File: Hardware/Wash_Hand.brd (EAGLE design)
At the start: 71.1 x 48.3 mm, 71 parts, among them IC1 LM358D, IC2 LP298XS, IC3 405016TSSOP, J1 I2C, J2 ICSP, J3 SPI, J4 9V_CONN, J5 EXT_VCC, J6 6_PIN_SERIAL_CABLEPTH, Q1 16.0 Mhz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

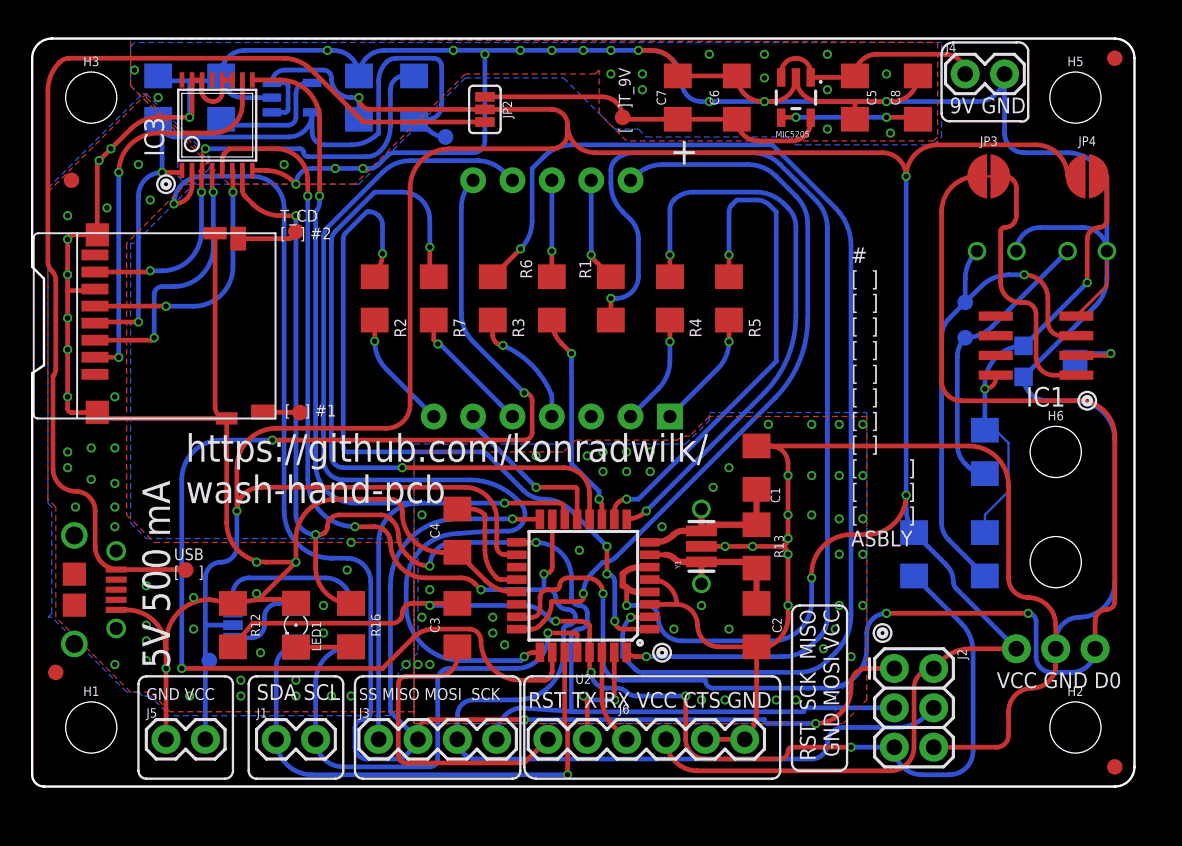
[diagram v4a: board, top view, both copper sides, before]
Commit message: Board: Fixup the registers name and values.
Align the names and values to be next to each other.

Signed-off-by: Konrad Rzeszutek Wilk <konrad@kernel.org>
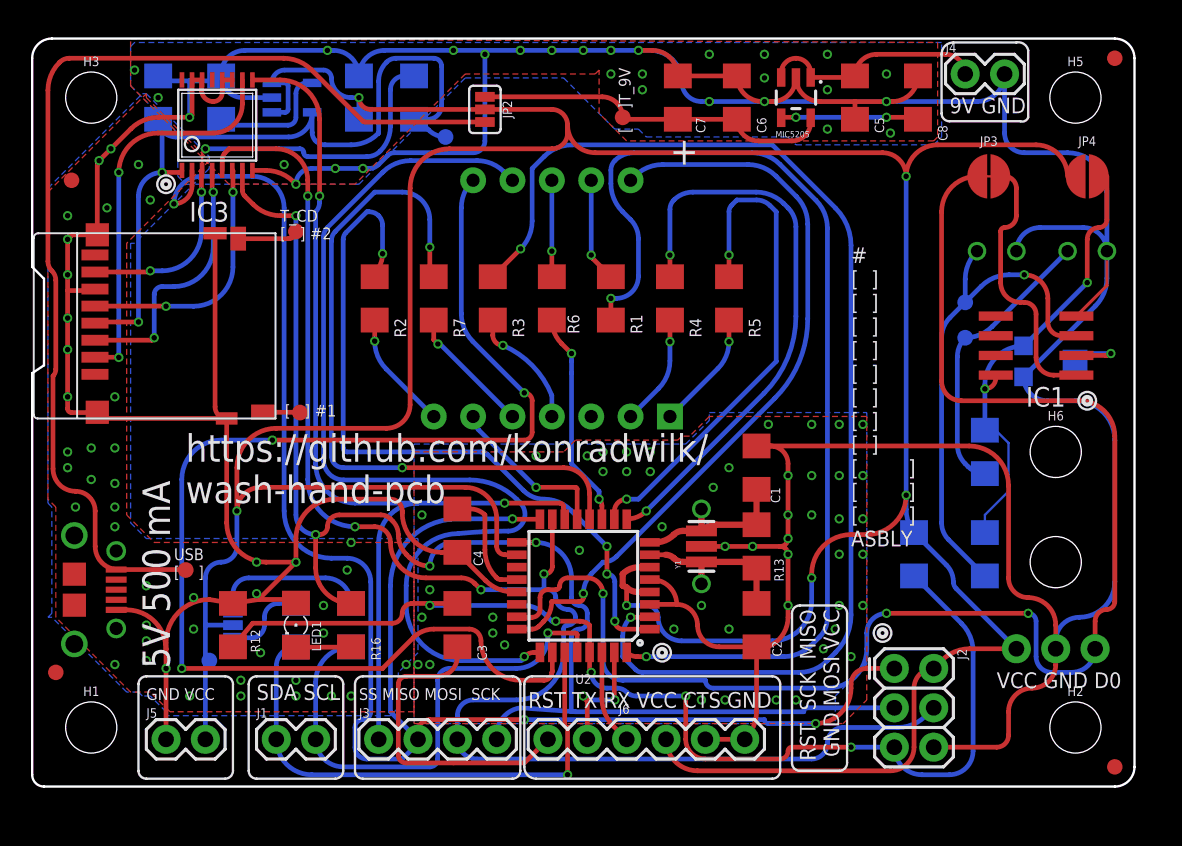
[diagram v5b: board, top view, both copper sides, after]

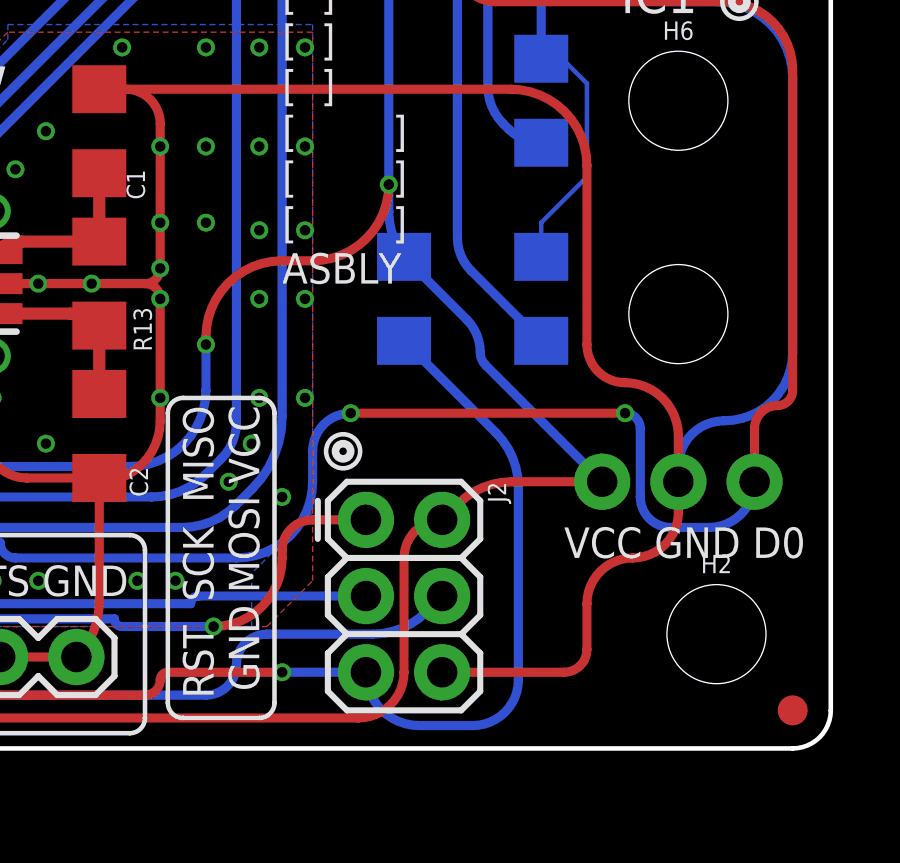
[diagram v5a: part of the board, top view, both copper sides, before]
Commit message: Board: Flip R9 around.
We don't want too many optional components on the back
to easy the production runs (as we have to use red
resin to glue it).

Signed-off-by: Konrad Rzeszutek Wilk <konrad@kernel.org>
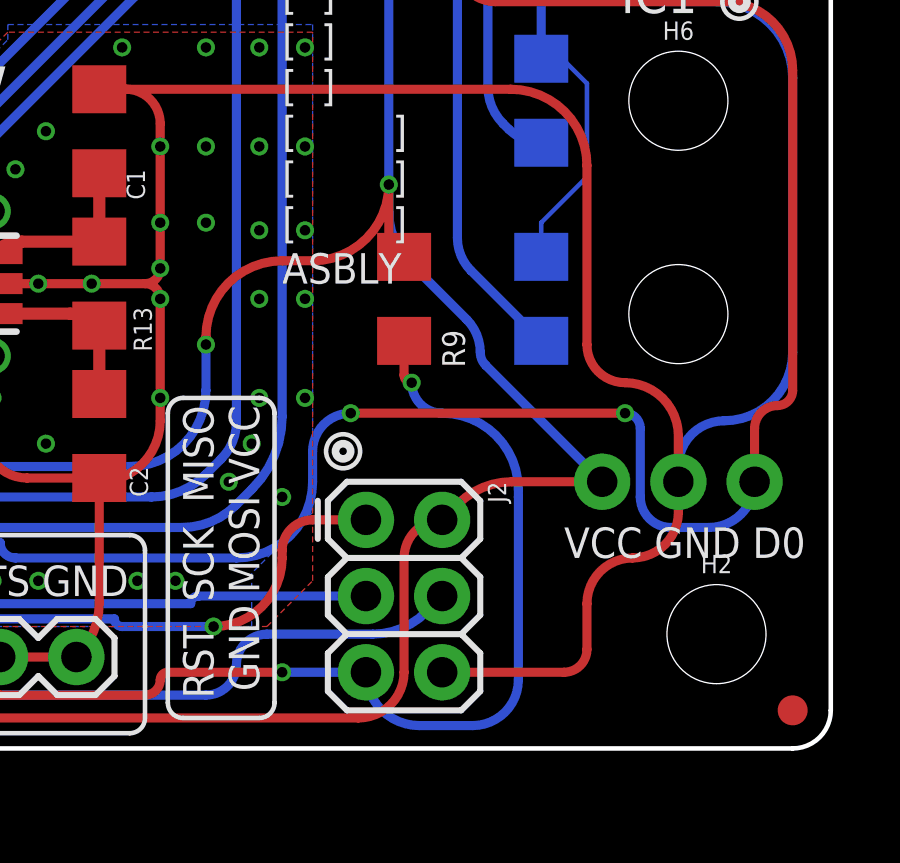
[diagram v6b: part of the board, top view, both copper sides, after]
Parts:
- flipped R9 to the top
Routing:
- net VCC: track 233.9 -> 236.3 mm
- net RESET: track 72.5 -> 72.6 mm, vias 5 -> 6
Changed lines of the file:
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@@
 <attribute name="VALUE" x="27.178" y="33.528" size="0.6096" layer="27" ratio="20" rot="R270"/>
 </element>
-<element name="R9" library="darnok_common" package="1206" value="10K" x="56.896" y="14.986" smashed="yes" rot="MR90">
-<attribute name="NAME" x="54.864" y="12.7" size="0.762" layer="26" ratio="24" rot="MR90"/>
-<attribute name="VALUE" x="55.118" y="15.748" size="0.6096" layer="28" ratio="20" rot="MR90"/>
+<element name="R9" library="darnok_common" package="1206" value="10K" x="56.896" y="14.986" smashed="yes" rot="R90">
+<attribute name="NAME" x="58.928" y="12.7" size="0.762" layer="25" ratio="24" rot="R90"/>
+<attribute name="VALUE" x="58.674" y="15.748" size="0.6096" layer="27" ratio="20" rot="R90"/>
 </element>
 <element name="U$4" library="darnok_usb" package="USB_MICROB_10118194_AMPHENOL" package3d_urn="urn:adsk.eagle:package:21769933/1" value="USB_MICROB_10118194_AMPHENOL" x="1.27" y="12.7" smashed="yes" rot="R270"/>
@@
 <contactref element="J2" pad="5"/>
 <contactref element="R12" pad="2"/>
-<wire x1="60.706" y1="8.723896875" x2="59.96205" y2="10.51995" width="0.3048" layer="16" curve="45"/>
-<wire x1="59.96205" y1="10.51995" x2="56.896" y2="13.586" width="0.3048" layer="16"/>
-<wire x1="60.706" y1="2.286" x2="60.706" y2="8.723896875" width="0.3048" layer="16"/>
+<wire x1="60.706" y1="2.286" x2="60.706" y2="8.382" width="0.3048" layer="16"/>
 <wire x1="23.238" y1="10.538" x2="14.224" y2="10.538" width="0.3048" layer="1"/>
 <wire x1="12.954" y1="9.014" x2="14.224" y2="10.538" width="0.3048" layer="1"/>
@@
 <wire x1="23.876" y1="11.176" x2="23.238" y2="10.538" width="0.3048" layer="1" curve="-90"/>
 <wire x1="25.524" y1="11.814" x2="24.514" y2="11.814" width="0.3048" layer="1"/>
+<wire x1="60.706" y1="8.382" x2="60.706" y2="8.636" width="0.3048" layer="16"/>
+<wire x1="60.706" y1="8.636" x2="58.166" y2="11.176" width="0.3048" layer="16" curve="90"/>
+<wire x1="58.166" y1="11.176" x2="57.15" y2="12.192" width="0.3048" layer="16" curve="-90"/>
+<via x="57.15" y="12.192" extent="1-16" drill="0.35"/>
+<wire x1="57.15" y1="12.192" x2="56.896" y2="12.446" width="0.3048" layer="1" curve="-90"/>
+<wire x1="56.896" y1="12.446" x2="56.896" y2="13.586" width="0.3048" layer="1"/>
 </signal>
 <signal name="VCC">
@@
 <wire x1="58.69205" y1="8.14605" x2="60.488103125" y2="8.89" width="0.3048" layer="1" curve="-45"/>
 <wire x1="60.488103125" y1="8.89" x2="63.5" y2="8.89" width="0.3048" layer="1"/>
-<wire x1="56.896" y1="16.386" x2="57.088" y2="16.194" width="0.3048" layer="16"/>
 <wire x1="57.088" y1="16.194" x2="58.984865625" y2="14.297134375" width="0.3048" layer="16"/>
 <wire x1="58.984865625" y1="14.297134375" x2="59.436" y2="13.208" width="0.3048" layer="16" curve="-45"/>
@@
 <wire x1="64.77" y1="41.402" x2="66.802" y2="39.37" width="0.3048" layer="1" curve="-90"/>
 <wire x1="58.42" y1="41.402" x2="64.77" y2="41.402" width="0.3048" layer="1"/>
+<wire x1="56.388" y1="18.796" x2="56.388" y2="16.894" width="0.3048" layer="1"/>
+<wire x1="56.388" y1="16.894" x2="56.896" y2="16.386" width="0.3048" layer="1" curve="90"/>
 </signal>
 <signal name="0">

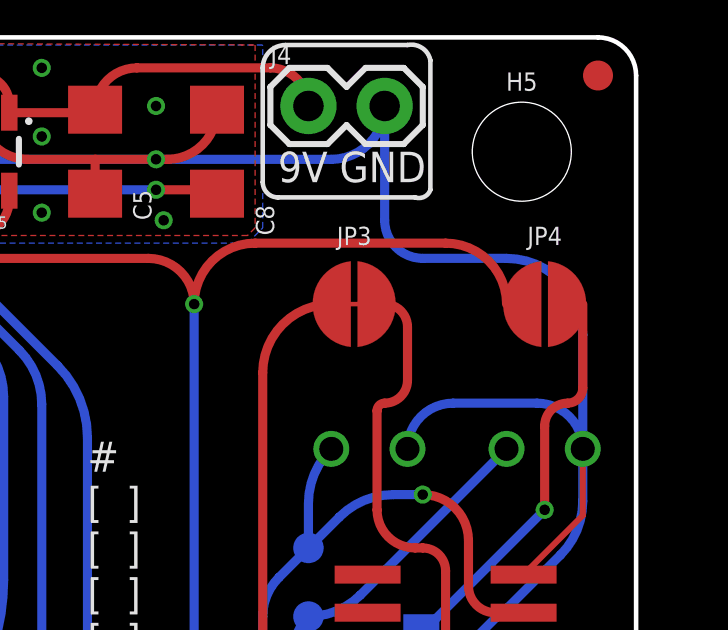
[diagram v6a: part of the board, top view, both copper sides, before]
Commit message: Board/Schematic: Replace open with closed SMT pads for line sensor
As we want it by default enabled.

Signed-off-by: Konrad Rzeszutek Wilk <konrad@kernel.org>
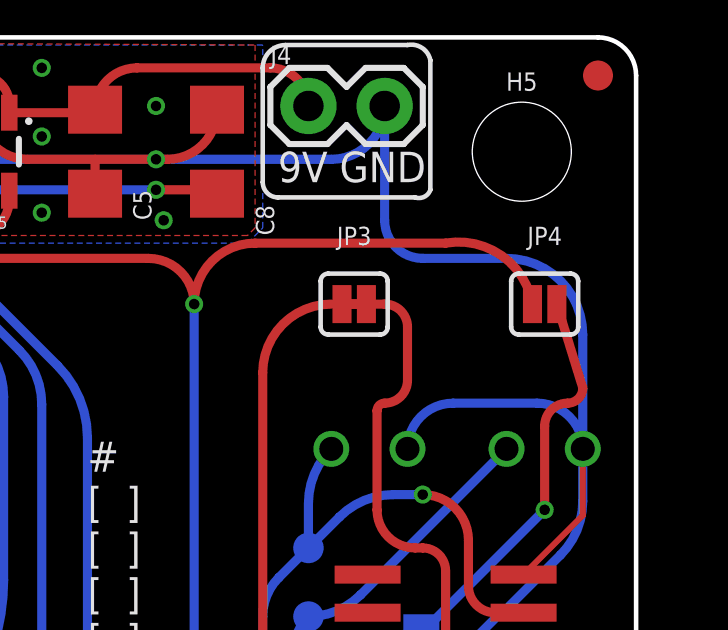
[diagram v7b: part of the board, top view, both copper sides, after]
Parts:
- JP3, JP4: device SparkFun-Jumpers:SMT-JUMPER_2_NO_NO-SILK_ROUND -> SparkFun-Jumpers:SMT-JUMPER_2_NC_PASTE_SILK
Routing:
- net VCC: track 236.3 -> 237.0 mm
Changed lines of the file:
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@@
 <attribute name="VALUE" x="27.432" y="43.688" size="0.6096" layer="27" font="vector" ratio="20" rot="R90" align="top-center"/>
 </element>
-<element name="JP3" library="SparkFun-Jumpers" library_urn="urn:adsk.eagle:library:528" package="SMT-JUMPER_2_NO_NO-SILK_ROUND" package3d_urn="urn:adsk.eagle:package:39278/1" value="ENA_INT_D0" x="61.722" y="39.37" smashed="yes">
+<element name="JP3" library="SparkFun-Jumpers" library_urn="urn:adsk.eagle:library:528" package="SMT-JUMPER_2_NC_PASTE_SILK" package3d_urn="urn:adsk.eagle:package:39282/1" value="ENA_INT_D0" x="61.722" y="39.37" smashed="yes">
 <attribute name="NAME" x="61.722" y="41.3385" size="0.6096" layer="25" font="vector" ratio="20" align="bottom-center"/>
 <attribute name="VALUE" x="61.722" y="37.4015" size="0.6096" layer="27" font="vector" ratio="20" align="top-center"/>
 </element>
-<element name="JP4" library="SparkFun-Jumpers" library_urn="urn:adsk.eagle:library:528" package="SMT-JUMPER_2_NO_NO-SILK_ROUND" package3d_urn="urn:adsk.eagle:package:39278/1" value="ENA_INT_SENSOR" x="68.072" y="39.37" smashed="yes">
+<element name="JP4" library="SparkFun-Jumpers" library_urn="urn:adsk.eagle:library:528" package="SMT-JUMPER_2_NC_PASTE_SILK" package3d_urn="urn:adsk.eagle:package:39282/1" value="ENA_INT_SENSOR" x="68.072" y="39.37" smashed="yes">
 <attribute name="NAME" x="68.072" y="41.3385" size="0.6096" layer="25" font="vector" ratio="20" align="bottom-center"/>
 <attribute name="VALUE" x="68.072" y="37.4015" size="0.6096" layer="27" font="vector" ratio="20" align="top-center"/>
@@
 <wire x1="52.832" y1="16.256" x2="53.848" y2="16.256" width="0.3048" layer="1"/>
 <wire x1="56.388" y1="39.37" x2="58.42" y2="41.402" width="0.3048" layer="1" curve="-90"/>
-<wire x1="64.77" y1="41.402" x2="66.802" y2="39.37" width="0.3048" layer="1" curve="-90"/>
+<wire x1="64.77" y1="41.402" x2="67.6656" y2="39.37" width="0.3048" layer="1" curve="-90"/>
 <wire x1="58.42" y1="41.402" x2="64.77" y2="41.402" width="0.3048" layer="1"/>
 <wire x1="56.388" y1="18.796" x2="56.388" y2="16.894" width="0.3048" layer="1"/>
@@
 <wire x1="67.31" y1="26.543" x2="67.37" y2="26.543" width="0.1524" layer="1"/>
 <contactref element="JP3" pad="2"/>
-<wire x1="60.452" y1="39.37" x2="60.96" y2="39.37" width="0.1524" layer="1"/>
-<wire x1="60.96" y1="39.37" x2="62.738" y2="39.37" width="0.1524" layer="1"/>
-<wire x1="62.738" y1="39.37" x2="62.992" y2="39.37" width="0.1524" layer="1"/>
+<wire x1="61.3156" y1="39.37" x2="60.96" y2="39.37" width="0.1524" layer="1"/>
 <wire x1="31.34465625" y1="10.922" x2="31.2674" y2="10.954" width="0.3048" layer="1" curve="-45"/>
 <wire x1="68.58" y1="8.89" x2="67.056" y2="7.366" width="0.3048" layer="16" curve="-90"/>
@@
 <wire x1="58.674" y1="37.084" x2="60.96" y2="39.37" width="0.3048" layer="1" curve="-90"/>
 <wire x1="58.674" y1="26.162" x2="58.674" y2="37.084" width="0.3048" layer="1"/>
+<wire x1="61.3156" y1="39.37" x2="62.738" y2="39.37" width="0.3048" layer="1"/>
+<wire x1="62.1284" y1="39.37" x2="61.3156" y2="39.37" width="0.3048" layer="1"/>
 </signal>
 <signal name="SDA">
@@
 <wire x1="61.468" y1="25.939" x2="61.468" y2="25.654" width="0.3048" layer="16"/>
 <wire x1="61.468" y1="22.99" x2="61.468" y2="25.654" width="0.3048" layer="16"/>
-<wire x1="69.342" y1="39.37" x2="69.342" y2="36.576" width="0.3048" layer="1"/>
+<wire x1="68.4784" y1="39.37" x2="69.342" y2="36.576" width="0.3048" layer="1"/>
 <wire x1="69.342" y1="36.576" x2="68.834" y2="36.068" width="0.3048" layer="1" curve="-90"/>
 <wire x1="68.834" y1="36.068" x2="68.072" y2="35.306" width="0.3048" layer="1" curve="90"/>

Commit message: Board/Schematic: Replace 9V/5V SMT pad with normally closed
Makes it easier to debug as the solder will close both
of. But if we are doing production runs we would enable/disable
the connectors by not populating the components (like the
whole 9V power-plant).

Signed-off-by: Konrad Rzeszutek Wilk <konrad@kernel.org>
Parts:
- JP2: device SparkFun-Jumpers:SMT-JUMPER_3_1-NC_PASTE_SILK -> SparkFun-Jumpers:SMT-JUMPER_3_2-NC_PASTE_SILK
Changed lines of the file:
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@@
 <attribute name="VALUE" x="59.436" y="42.164" size="0.6096" layer="27" font="vector" ratio="20"/>
 </element>
-<element name="JP2" library="SparkFun-Jumpers" library_urn="urn:adsk.eagle:library:528" package="SMT-JUMPER_3_1-NC_PASTE_SILK" package3d_urn="urn:adsk.eagle:package:39293/1" value="9V_JUMPER" x="29.21" y="43.688" smashed="yes" rot="R270">
+<element name="JP2" library="SparkFun-Jumpers" library_urn="urn:adsk.eagle:library:528" package="SMT-JUMPER_3_2-NC_PASTE_SILK" package3d_urn="urn:adsk.eagle:package:39294/1" value="9V_JUMPER" x="29.21" y="43.688" smashed="yes" rot="R270">
 <attribute name="NAME" x="30.353" y="43.688" size="0.6096" layer="25" font="vector" ratio="20" rot="R270" align="bottom-center"/>
 <attribute name="VALUE" x="27.432" y="43.688" size="0.6096" layer="27" font="vector" ratio="20" rot="R90" align="top-center"/>
